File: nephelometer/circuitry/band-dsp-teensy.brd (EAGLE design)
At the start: 77 x 48 mm, 28 parts, among them IC1 AD822N, IC4 LM4041CILP, T1 2N2222, T2 2N2222

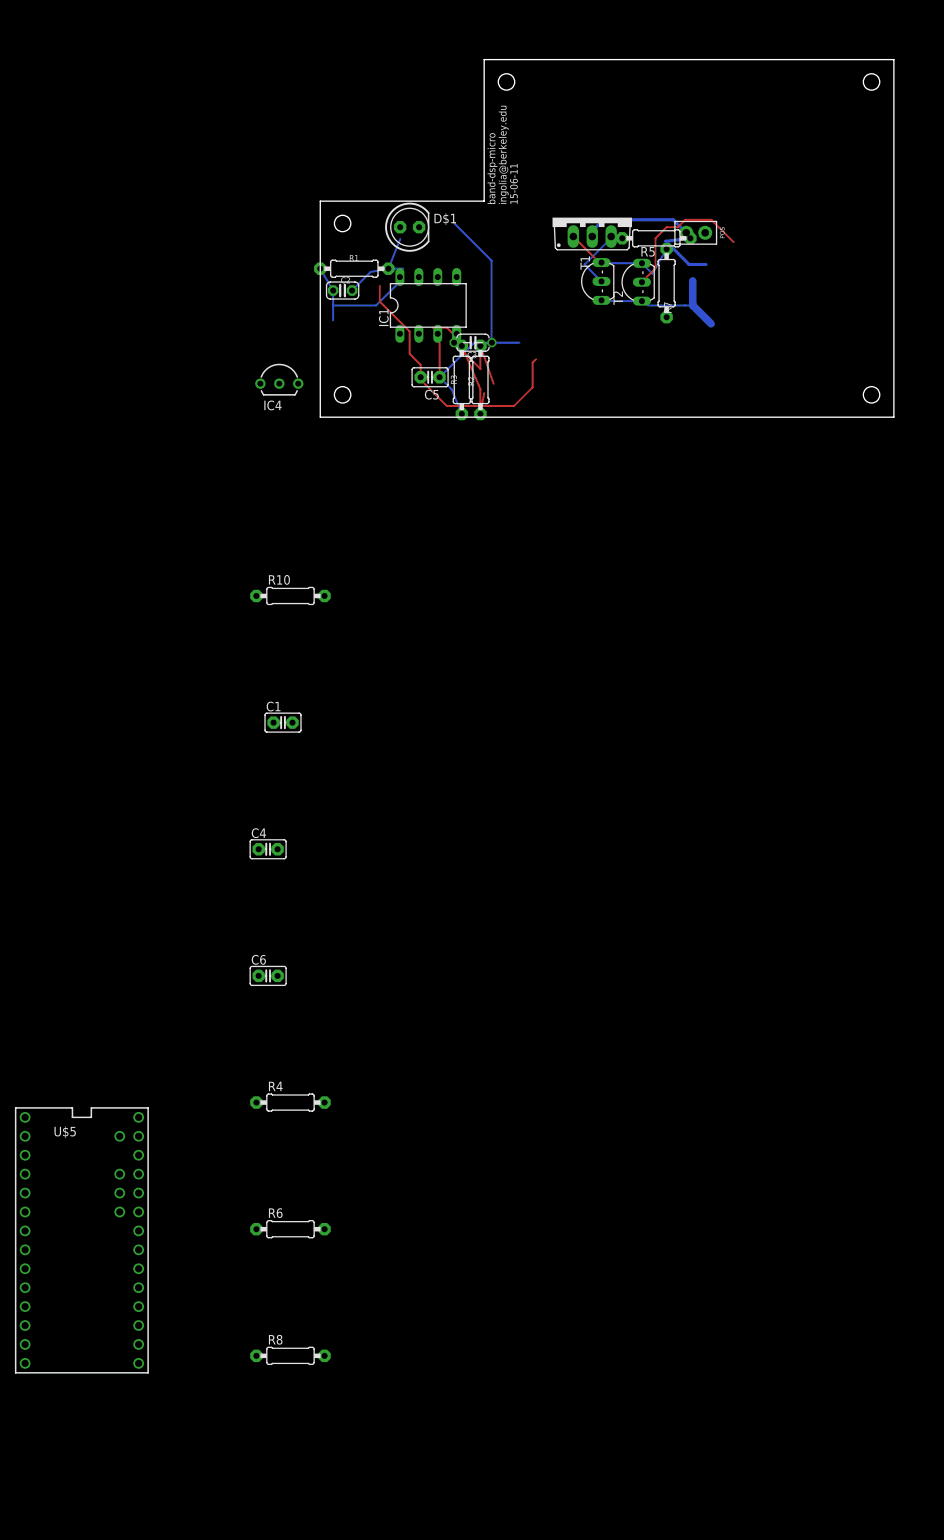
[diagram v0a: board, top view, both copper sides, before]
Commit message: programmable gain amplifier incorporated
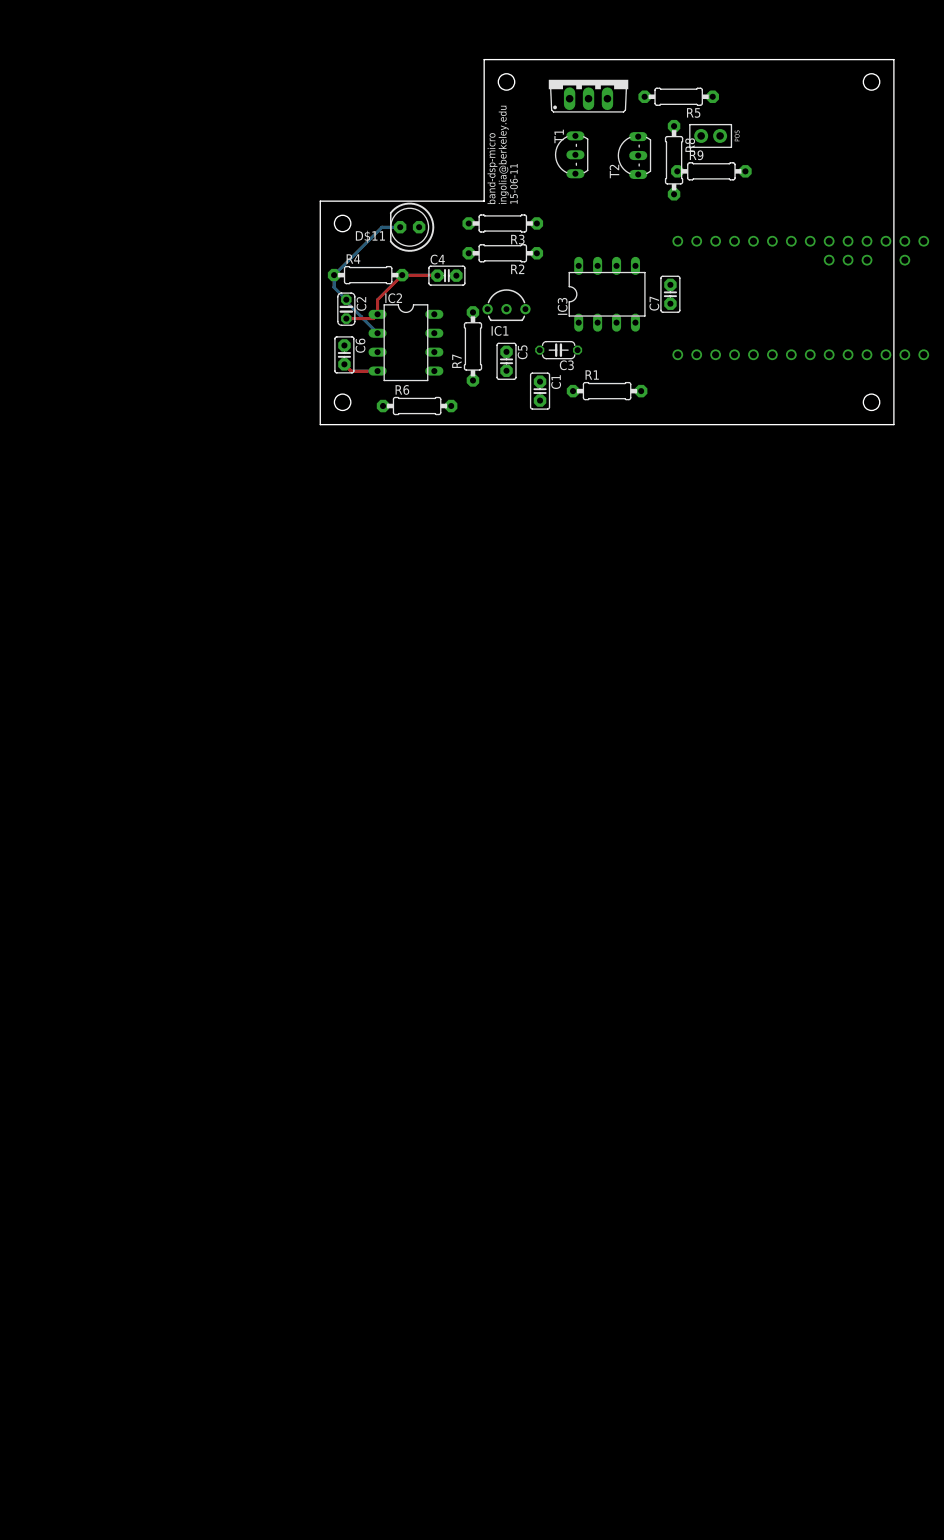
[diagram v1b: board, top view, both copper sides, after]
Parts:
- removed IC4: LM4041CILP, texas:LP_O-PBCY-W3
- removed Q2: (no value), ingolia:TO220BV
- removed R10: 330R, adafruit:0207/9
- removed U$5: TEENSY_3.1-3.2_DIL+4, Teensy_3_and_LC_Series_Boards_v1.4:TEENSY_3.0-3.2&LC_DIL+4
- added BRD1: TEENSY_3.1-3.2_DIL+4, Teensy_3_and_LC_Series_Boards_v1.4:TEENSY_3.0-3.2&LC_DIL+4
- added C7: 100nF, adafruit:C025-025X050
- added IC2: AD822N, analog-devices:DIL08
- added IC3: MCP6S21, ingolia:DIL08
- added Q1: (no value), ingolia:TO220BV
- added R9: 4K7, adafruit:0207/9
- C5: value 100nF -> 1.2pF
- C6: value 1.2pF -> 100nF
- IC1: value AD822N -> LM4041CILP; device analog-devices:DIL08 -> texas:LP_O-PBCY-W3
- R1: value 1M0 -> 330R
- R4: value 28k7 -> 1M0
- R6: value 14K3 -> 28k7
- R7: value 4K7 -> 14K3
- moved R8 168.5 mm to (47.5, 40.5), turned to 270 degrees
- moved R6 111.8 mm to (13.0, 7.50)
- moved R4 111.6 mm to (6.43, 25.1)
- moved C6 84.0 mm to (3.24, 14.4), turned to 270 degrees
- moved C4 80.7 mm to (17.0, 25.0)
- moved C1 56.3 mm to (29.5, 9.50), turned to 270 degrees
- moved R1 37.7 mm to (38.5, 9.50), turned to 0 degrees
- moved R7 27.3 mm to (20.5, 15.5), turned to 90 degrees
- moved R3 21.7 mm to (24.5, 32.0), turned to 180 degrees
- moved R5 19.2 mm to (48.1, 49.0)
- moved T1 17.4 mm to (33.0, 41.2)
- moved R2 17.3 mm to (24.5, 28.0), turned to 180 degrees
- moved T2 17.0 mm to (41.4, 41.1)
- moved JP1 13.2 mm to (54.9, 45.0)
- moved C3 11.5 mm to (32.0, 15.0), turned to 180 degrees
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- renumbered D$1 to D$11
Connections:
- removed net N$10: IC1.6, IC1.7, R6.1, U$5.A10
- new net CS_PGA: BRD1.15/A1, IC3.5
- new net MOSI: BRD1.11, IC3.6
- new net N$3: IC2.6, IC2.7, IC3.2, R7.1
- new net N$4: BRD1.A10, IC3.1
- new net SCK: BRD1.13, IC3.7
- net +3V3: now also BRD1.3.3V, C6.1, C7.2, IC2.8, IC3.8, R1.2; no longer C5.1, IC1.8, R10.2, U$5.3.3V
- net +5V: now also BRD1.VIN, R8.2; no longer R7.2, U$5.VIN
- net 1V65: now also BRD1.A11, IC1.2, IC2.3, IC3.3, R1.1, R6.1; no longer IC1.3, IC4.2, R10.1, R4.1, U$5.A11
- net AGND: now also BRD1.AGND; no longer U$5.AGND
- net AREF: now also BRD1.AREF; no longer U$5.AREF
- net GND: now also BRD1.GND, C6.2, C7.1, IC1.3, IC2.4, IC3.4; no longer C5.2, IC1.4, IC4.3, U$5.GND
- net LEDCTRL: now also R9.2; no longer R8.2
- net N$1: now also IC2.2, R4.1; no longer IC1.2, R1.1
- net N$14: now also Q1.S; no longer Q2.S
- net N$18: now also Q1.D; no longer Q2.D
- net N$2: now also C5.1, R7.2; no longer C6.1, R6.2
- net N$22: now also IC2.1, R4.2; no longer IC1.1, R1.2
- net N$35: now also IC1.1; no longer IC4.1
- net N$5: now also BRD1.2, R9.1; no longer R8.1, U$5.2
- net N$8: now also Q1.G, R8.1; no longer Q2.G, R7.1
- net N$9: now also C5.2, IC2.5, R6.2; no longer C6.2, IC1.5, R4.2
- net VUSB: now also BRD1.VUSB; no longer U$5.VUSB
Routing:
- net GND: track 70.5 -> 4.82 mm
- net +3V3: track 36.3 -> 0.00 mm
- net LEDCTRL: track 19.4 -> 0.00 mm
- net 1V65: track 18.1 -> 0.00 mm
- net N$8: track 16.5 -> 0.00 mm
- net N$18: track 14.7 -> 0.00 mm
- net N$35: track 12.5 -> 0.00 mm
- net N$14: track 10.0 -> 0.00 mm
- net N$1: track 12.2 -> 21.8 mm
- net N$22: track 17.1 -> 15.8 mm
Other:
- board size 77 x 48 mm -> 77 x 49 mm

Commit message: Stackable motor controller board w/ 3.3V control; USB versus wall power; test order for components
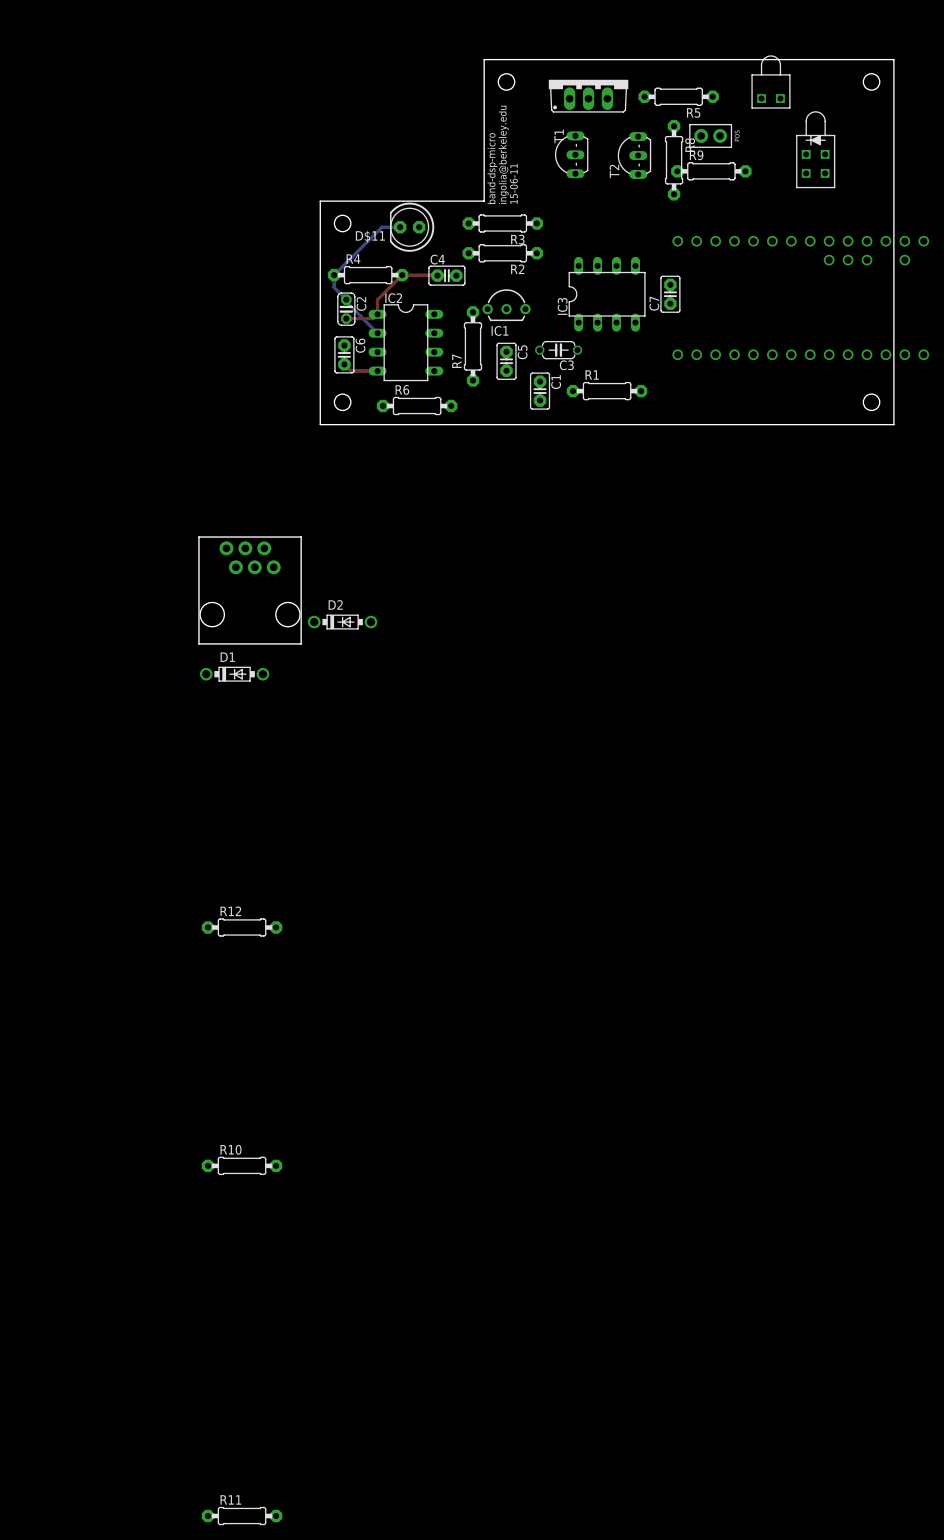
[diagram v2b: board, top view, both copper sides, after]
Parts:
- added D1, D2: 1N5817-T, diode:DO41-7.6
- added J1: RJ11-6PTH, SparkFun-Connectors:RJ11-6
- added R10, R11: 330R, adafruit:0207/9
- added R12: 150R, adafruit:0207/9
- added U$5: LED3MM-BILEV-INDIC, ingolia:LED3MM-BILEV-INDIC
- added U$6: LED3MM-RG-INDIC, ingolia:LED3MM-INDIC
- Q1: value (none) -> IRLB8721
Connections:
- removed net VUSB: BRD1.VUSB
- new net MOT1: BRD1.16/A2, J1.4
- new net MOT2: BRD1.17/A3, J1.3
- new net N$10: D2.A, J1.5, U$6.1
- new net N$11: R12.2, U$5.AT
- new net N$12: R11.2, U$6.2
- new net N$7: R10.2, U$5.CB
- new net V+: BRD1.VUSB, D1.A
- net +3V3: now also R12.1
- net +5V: now also D1.C, D2.C, U$5.AB
- net GND: now also J1.2, R10.1, R11.1
- net N$5: now also U$5.CT

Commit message: Laid out circuit for teensy nephelometer
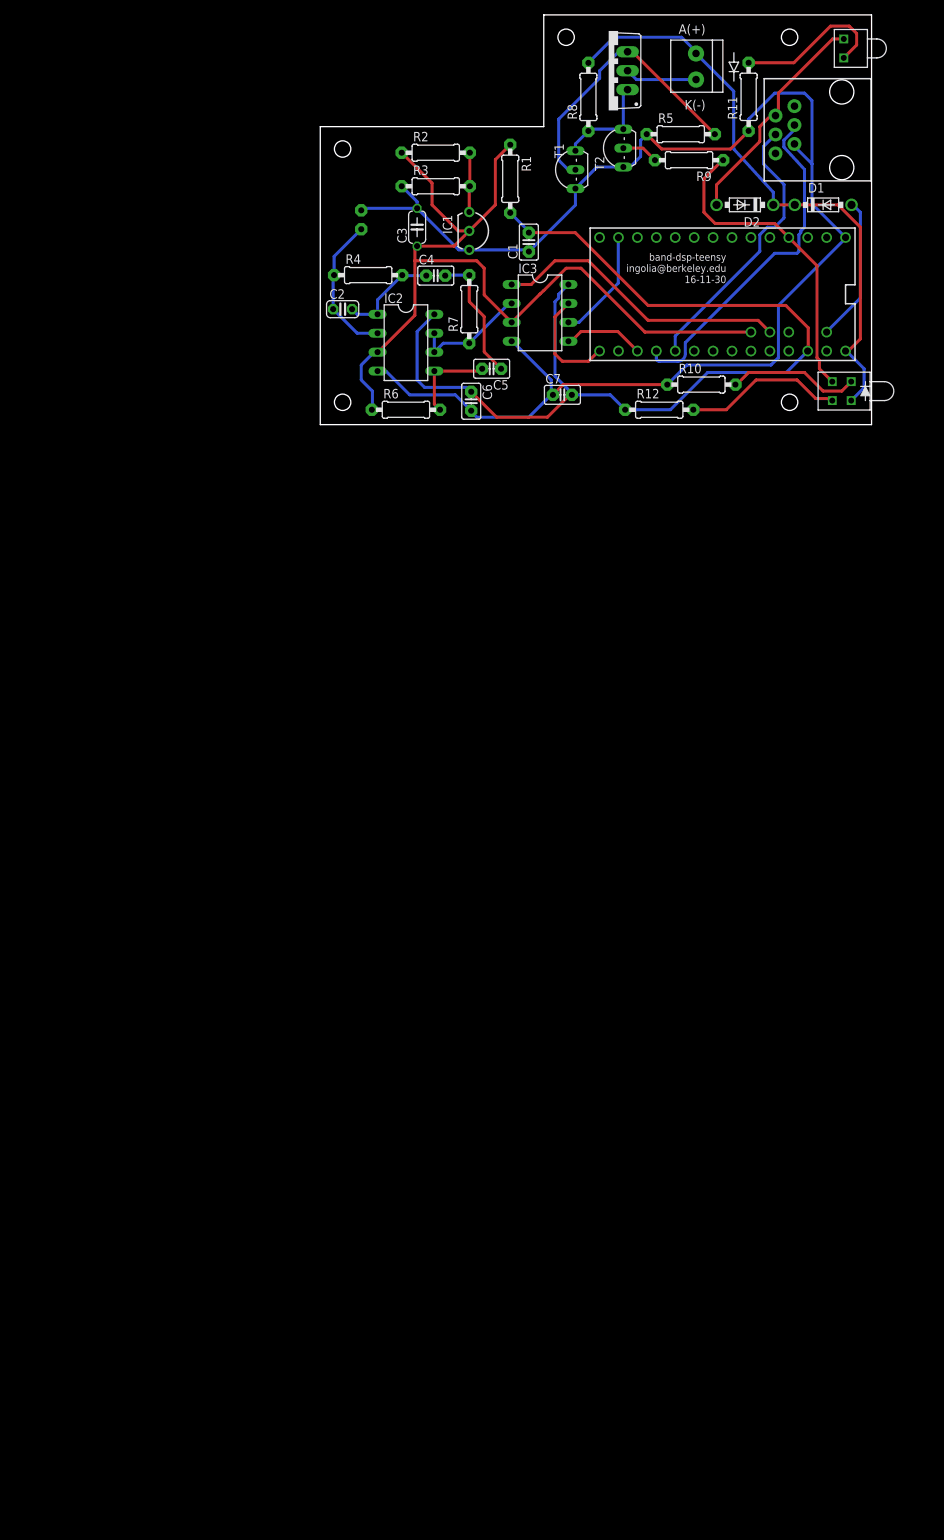
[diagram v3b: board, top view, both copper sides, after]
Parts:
- JP1: device ingolia:1X02_SCREW -> ingolia:1X02_3.5MM
- moved R11 202.3 mm to (57.5, 49.0), turned to 90 degrees
- moved R10 121.7 mm to (51.2, 10.4)
- moved J1 103.6 mm to (70.0, 39.5), turned to 90 degrees
- moved D1 101.0 mm to (67.5, 34.5)
- moved R12 89.3 mm to (45.5, 7.00)
- moved D2 77.8 mm to (57.0, 34.5), turned to 180 degrees
- moved R1 31.3 mm to (25.5, 38.0), turned to 270 degrees
- moved U$5 30.7 mm to (70.0, 9.50), turned to 270 degrees
- moved C3 25.2 mm to (13.0, 31.5), turned to 90 degrees
- moved C1 20.1 mm to (28.0, 29.5), turned to 90 degrees
- moved C7 19.8 mm to (32.5, 9.00), turned to 0 degrees
- moved C6 18.1 mm to (20.3, 8.14)
- moved R2 16.2 mm to (15.5, 41.5), turned to 0 degrees
- moved R8 14.3 mm to (36.0, 49.0), turned to 90 degrees
- moved U$2 12.5 mm to (63.0, 57.0)
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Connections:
- net +5V: now also JP1.1A; no longer JP1.1/POS
- net N$18: now also JP1.2K; no longer JP1.2
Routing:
- net GND: track 4.82 -> 194.1 mm
- net +3V3: track 0.00 -> 135.8 mm
- net 1V65: track 0.00 -> 120.0 mm
- net +5V: track 0.00 -> 80.4 mm
- net MOT1: track 0.00 -> 46.2 mm
- net N$5: track 0.00 -> 42.7 mm
- net N$4: track 0.00 -> 39.9 mm
- net N$14: track 0.00 -> 38.2 mm
- net MOT2: track 0.00 -> 37.5 mm
- net N$10: track 0.00 -> 30.6 mm
- net N$11: track 0.00 -> 21.5 mm
- net N$12: track 0.00 -> 20.9 mm
- net V+: track 0.00 -> 19.6 mm
- net N$7: track 0.00 -> 17.8 mm
- net N$2: track 0.00 -> 17.6 mm
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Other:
- board size 77 x 49 mm -> 74 x 55 mm
- board text added: "band-dsp-teensy ingolia@berkeley.edu 16-11-30"
- board text removed: "band-dsp-micro ingolia@berkeley.edu 15-06-11"

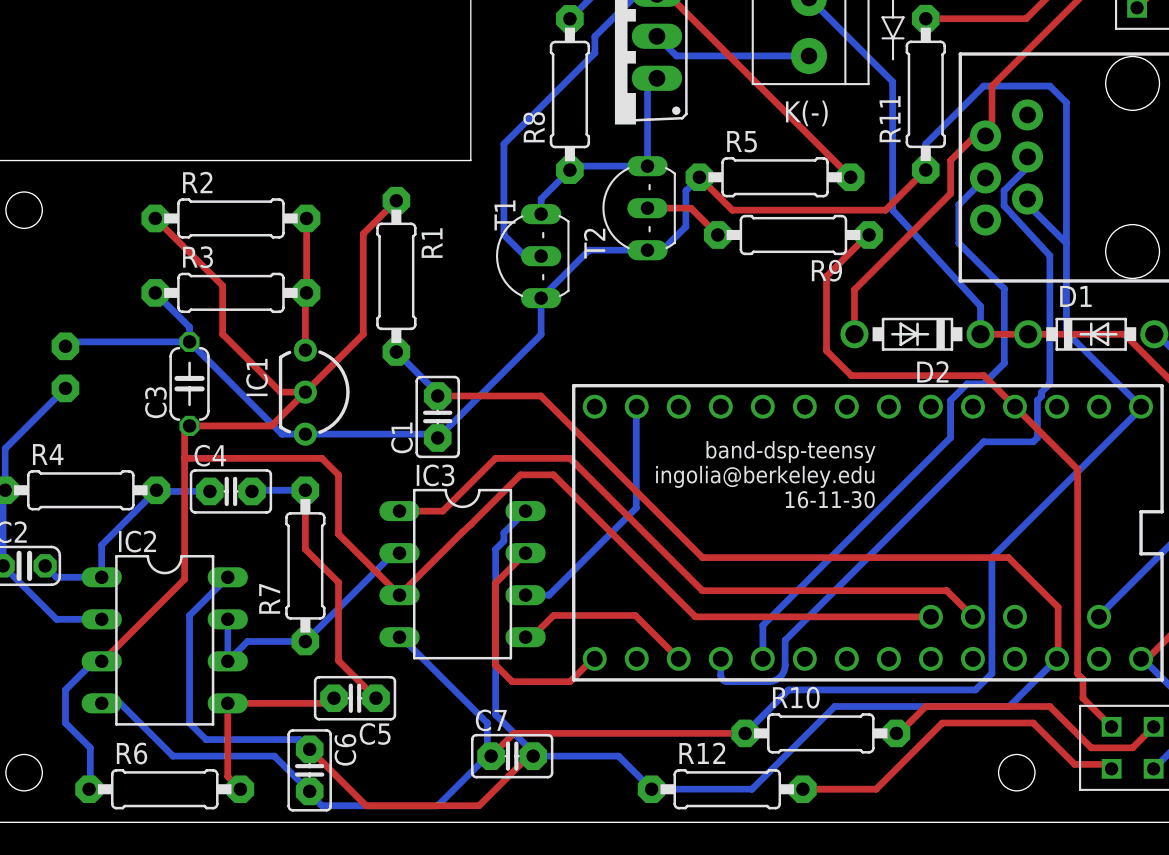
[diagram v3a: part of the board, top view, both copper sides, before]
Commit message: Designed motor power board to stack on nephelometer or run over RJ11 cable
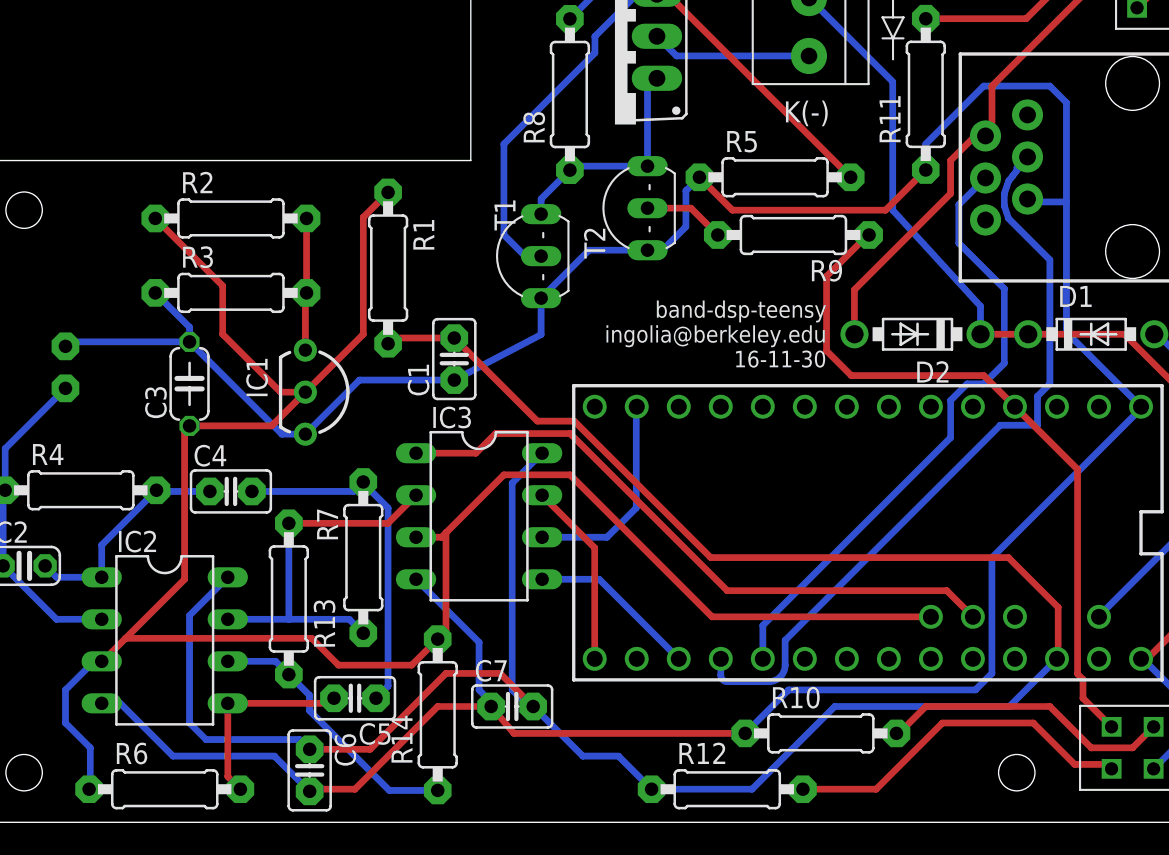
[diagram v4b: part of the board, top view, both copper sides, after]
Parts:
- added R13, R14: 14K3, adafruit:0207/9
- moved C1 3.64 mm to (29.0, 33.0)
- moved IC3 3.64 mm to (30.5, 23.5)
- moved R7 3.54 mm to (23.5, 21.0)
- moved C7 3.00 mm to (32.5, 12.0)
- moved R1 0.71 mm to (25.0, 38.5)
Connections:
- new net N$6: IC2.6, R13.2, R14.1
- net 1V65: now also R14.2
- net N$3: now also R13.1; no longer IC2.6
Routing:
- net N$6: track 0.00 -> 16.5 mm
- net N$3: track 15.6 -> 22.7 mm
- net 1V65: track 120.0 -> 126.2 mm
- net N$2: track 17.6 -> 21.0 mm
- net SCK: track 14.5 -> 11.2 mm
- net MOSI: track 15.0 -> 12.6 mm
- net +3V3: track 135.8 -> 138.2 mm
- net N$4: track 39.9 -> 38.7 mm
- net GND: track 194.1 -> 193.5 mm
- net CS_PGA: track 10.9 -> 10.3 mm
- net MOT1: track 46.2 -> 45.7 mm
